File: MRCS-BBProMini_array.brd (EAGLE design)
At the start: 107.5 x 110 mm, 30 parts

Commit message: fixed silkscreen
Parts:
- ARDUINO1X11, ARDUINO1X12, ARDUINO1X13: value (none) -> ARDUINO_PRO_MINI_DAVEK
- BBLEOX11, BBLEOX12, BBLEOX13: value (none) -> Footprint
- C1X11, C1X12, C1X13: device SPCoast:e5-10.5 -> SPCoast:E5-10.5
- C2X11, C2X12, C2X13: value (none) -> 1.0uF
- C3X11, C3X12, C3X13: value (none) -> 10uF
- J1X11, J1X12, J1X13: value (none) -> 2.1mm
- VR5.0X11, VR5.0X12, VR5.0X13: value (none) -> 5v
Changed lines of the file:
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@@
 <layer number="23" name="tOrigins" color="15" fill="1" visible="yes" active="yes"/>
 <layer number="24" name="bOrigins" color="15" fill="1" visible="no" active="yes"/>
-<layer number="25" name="tNames" color="7" fill="1" visible="no" active="yes"/>
+<layer number="25" name="tNames" color="7" fill="1" visible="yes" active="yes"/>
 <layer number="26" name="bNames" color="7" fill="1" visible="no" active="yes"/>
-<layer number="27" name="tValues" color="7" fill="1" visible="no" active="yes"/>
+<layer number="27" name="tValues" color="7" fill="1" visible="yes" active="yes"/>
 <layer number="28" name="bValues" color="7" fill="1" visible="no" active="yes"/>
 <layer number="29" name="tStop" color="7" fill="3" visible="no" active="yes"/>
@@
 <layer number="46" name="Milling" color="3" fill="1" visible="yes" active="yes"/>
 <layer number="47" name="Measures" color="7" fill="1" visible="yes" active="yes"/>
-<layer number="48" name="Document" color="7" fill="1" visible="no" active="yes"/>
+<layer number="48" name="Document" color="7" fill="1" visible="yes" active="yes"/>
 <layer number="49" name="Reference" color="7" fill="1" visible="yes" active="yes"/>
 <layer number="50" name="dxf" color="7" fill="1" visible="no" active="no"/>
@@
 <layer number="102" name="Changes" color="13" fill="1" visible="yes" active="yes"/>
 <layer number="103" name="tMap" color="29" fill="4" visible="no" active="yes"/>
-<layer number="104" name="Name" color="16" fill="1" visible="no" active="yes"/>
+<layer number="104" name="Name" color="16" fill="1" visible="yes" active="yes"/>
 <layer number="105" name="tPlate" color="7" fill="1" visible="no" active="yes"/>
 <layer number="106" name="bPlate" color="7" fill="1" visible="no" active="yes"/>
@@
 <layer number="123" name="tTestmark" color="7" fill="1" visible="no" active="yes"/>
 <layer number="124" name="bTestmark" color="7" fill="1" visible="no" active="yes"/>
-<layer number="125" name="_tNames" color="14" fill="1" visible="yes" active="yes"/>
+<layer number="125" name="_tNames" color="14" fill="1" visible="no" active="yes"/>
 <layer number="126" name="_bNames" color="7" fill="1" visible="no" active="yes"/>
 <layer number="127" name="_tValues" color="7" fill="1" visible="no" active="no"/>
@@
 </autorouter>
 <elements>
-<element name="ARDUINO1X11" library="SPCoast" package="ARDUINO_PRO_MINI_DAVEK" value="" x="39.37" y="26.67" rot="R270"/>
-<element name="BBLEOX11" library="SPCoast" package="ARDUINO-BBLEO" value="" x="0" y="0"/>
-<element name="C1X11" library="SPCoast" package="e5-10.5" value="" x="15.875" y="18.415" rot="R90"/>
-<element name="C2X11" library="SPCoast" package="C050-024X044" value="" x="3.175" y="27.305" rot="R90"/>
-<element name="C3X11" library="SPCoast" package="C050-024X044" value="" x="3.175" y="19.685" rot="R270"/>
-<element name="J1X11" library="SPCoast" package="DCJ0202" value="" x="8.89" y="9.525" rot="R270"/>
+<element name="ARDUINO1X11" library="SPCoast" package="ARDUINO_PRO_MINI_DAVEK" value="ARDUINO_PRO_MINI_DAVEK" x="39.37" y="26.67" rot="R270"/>
+<element name="BBLEOX11" library="SPCoast" package="ARDUINO-BBLEO" value="Footprint" x="0" y="0"/>
+<element name="C1X11" library="SPCoast" package="E5-10.5" value="" x="15.875" y="18.415" rot="R90"/>
+<element name="C2X11" library="SPCoast" package="C050-024X044" value="1.0uF" x="3.175" y="27.305" rot="R90"/>
+<element name="C3X11" library="SPCoast" package="C050-024X044" value="10uF" x="3.175" y="19.685" rot="R270"/>
+<element name="J1X11" library="SPCoast" package="DCJ0202" value="2.1mm" x="8.89" y="9.525" rot="R270"/>
 <element name="JP1X11" library="SPCoast" package="SJ_2S-NO" value="" x="60.96" y="4.445" rot="R90"/>
 <element name="LABEL1X11" library="SPCoast" package="PWR_LABEL" value="" x="20.32" y="6.985" rot="R90"/>
 <element name="OSHW1X11" library="SPCoast" package="OSHW-LOGO-M" value="" x="34.29" y="11.43"/>
-<element name="VR5.0X11" library="SPCoast" package="TO-220-RA-SINK" value="" x="6.35" y="23.495" rot="R270"/>
-<element name="ARDUINO1X12" library="SPCoast" package="ARDUINO_PRO_MINI_DAVEK" value="" x="39.37" y="59.944" rot="R270"/>
-<element name="BBLEOX12" library="SPCoast" package="ARDUINO-BBLEO" value="" x="0" y="33.274"/>
-<element name="C1X12" library="SPCoast" package="e5-10.5" value="" x="15.875" y="51.689" rot="R90"/>
-<element name="C2X12" library="SPCoast" package="C050-024X044" value="" x="3.175" y="60.579" rot="R90"/>
-<element name="C3X12" library="SPCoast" package="C050-024X044" value="" x="3.175" y="52.959" rot="R270"/>
-<element name="J1X12" library="SPCoast" package="DCJ0202" value="" x="8.89" y="42.799" rot="R270"/>
+<element name="VR5.0X11" library="SPCoast" package="TO-220-RA-SINK" value="5v" x="6.35" y="23.495" rot="R270"/>
+<element name="ARDUINO1X12" library="SPCoast" package="ARDUINO_PRO_MINI_DAVEK" value="ARDUINO_PRO_MINI_DAVEK" x="39.37" y="59.944" rot="R270"/>
+<element name="BBLEOX12" library="SPCoast" package="ARDUINO-BBLEO" value="Footprint" x="0" y="33.274"/>
+<element name="C1X12" library="SPCoast" package="E5-10.5" value="" x="15.875" y="51.689" rot="R90"/>
+<element name="C2X12" library="SPCoast" package="C050-024X044" value="1.0uF" x="3.175" y="60.579" rot="R90"/>
+<element name="C3X12" library="SPCoast" package="C050-024X044" value="10uF" x="3.175" y="52.959" rot="R270"/>
+<element name="J1X12" library="SPCoast" package="DCJ0202" value="2.1mm" x="8.89" y="42.799" rot="R270"/>
 <element name="JP1X12" library="SPCoast" package="SJ_2S-NO" value="" x="60.96" y="37.719" rot="R90"/>
 <element name="LABEL1X12" library="SPCoast" package="PWR_LABEL" value="" x="20.32" y="40.259" rot="R90"/>
 <element name="OSHW1X12" library="SPCoast" package="OSHW-LOGO-M" value="" x="34.29" y="44.704"/>
-<element name="VR5.0X12" library="SPCoast" package="TO-220-RA-SINK" value="" x="6.35" y="56.769" rot="R270"/>
-<element name="ARDUINO1X13" library="SPCoast" package="ARDUINO_PRO_MINI_DAVEK" value="" x="39.37" y="93.218" rot="R270"/>
-<element name="BBLEOX13" library="SPCoast" package="ARDUINO-BBLEO" value="" x="0" y="66.548"/>
-<element name="C1X13" library="SPCoast" package="e5-10.5" value="" x="15.875" y="84.963" rot="R90"/>
-<element name="C2X13" library="SPCoast" package="C050-024X044" value="" x="3.175" y="93.853" rot="R90"/>
-<element name="C3X13" library="SPCoast" package="C050-024X044" value="" x="3.175" y="86.233" rot="R270"/>
-<element name="J1X13" library="SPCoast" package="DCJ0202" value="" x="8.89" y="76.073" rot="R270"/>
+<element name="VR5.0X12" library="SPCoast" package="TO-220-RA-SINK" value="5v" x="6.35" y="56.769" rot="R270"/>
+<element name="ARDUINO1X13" library="SPCoast" package="ARDUINO_PRO_MINI_DAVEK" value="ARDUINO_PRO_MINI_DAVEK" x="39.37" y="93.218" rot="R270"/>
+<element name="BBLEOX13" library="SPCoast" package="ARDUINO-BBLEO" value="Footprint" x="0" y="66.548"/>
+<element name="C1X13" library="SPCoast" package="E5-10.5" value="" x="15.875" y="84.963" rot="R90"/>
+<element name="C2X13" library="SPCoast" package="C050-024X044" value="1.0uF" x="3.175" y="93.853" rot="R90"/>
+<element name="C3X13" library="SPCoast" package="C050-024X044" value="10uF" x="3.175" y="86.233" rot="R270"/>
+<element name="J1X13" library="SPCoast" package="DCJ0202" value="2.1mm" x="8.89" y="76.073" rot="R270"/>
 <element name="JP1X13" library="SPCoast" package="SJ_2S-NO" value="" x="60.96" y="70.993" rot="R90"/>
 <element name="LABEL1X13" library="SPCoast" package="PWR_LABEL" value="" x="20.32" y="73.533" rot="R90"/>
 <element name="OSHW1X13" library="SPCoast" package="OSHW-LOGO-M" value="" x="34.29" y="77.978"/>
-<element name="VR5.0X13" library="SPCoast" package="TO-220-RA-SINK" value="" x="6.35" y="90.043" rot="R270"/>
+<element name="VR5.0X13" library="SPCoast" package="TO-220-RA-SINK" value="5v" x="6.35" y="90.043" rot="R270"/>
 </elements>
 <signals>

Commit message: fixed silkscreen
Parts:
- C1X11, C1X12, C1X13: value (none) -> 150uF
- JP1X11, JP1X12, JP1X13: value (none) -> OFF
- LABEL1X11, LABEL1X12, LABEL1X13: value (none) -> 7-12vDC
- OSHW1X11, OSHW1X12, OSHW1X13: value (none) -> OSHW
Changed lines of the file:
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@@
 <element name="ARDUINO1X11" library="SPCoast" package="ARDUINO_PRO_MINI_DAVEK" value="ARDUINO_PRO_MINI_DAVEK" x="39.37" y="26.67" rot="R270"/>
 <element name="BBLEOX11" library="SPCoast" package="ARDUINO-BBLEO" value="Footprint" x="0" y="0"/>
-<element name="C1X11" library="SPCoast" package="E5-10.5" value="" x="15.875" y="18.415" rot="R90"/>
+<element name="C1X11" library="SPCoast" package="E5-10.5" value="150uF" x="15.875" y="18.415" rot="R90"/>
 <element name="C2X11" library="SPCoast" package="C050-024X044" value="1.0uF" x="3.175" y="27.305" rot="R90"/>
 <element name="C3X11" library="SPCoast" package="C050-024X044" value="10uF" x="3.175" y="19.685" rot="R270"/>
 <element name="J1X11" library="SPCoast" package="DCJ0202" value="2.1mm" x="8.89" y="9.525" rot="R270"/>
-<element name="JP1X11" library="SPCoast" package="SJ_2S-NO" value="" x="60.96" y="4.445" rot="R90"/>
-<element name="LABEL1X11" library="SPCoast" package="PWR_LABEL" value="" x="20.32" y="6.985" rot="R90"/>
-<element name="OSHW1X11" library="SPCoast" package="OSHW-LOGO-M" value="" x="34.29" y="11.43"/>
+<element name="JP1X11" library="SPCoast" package="SJ_2S-NO" value="OFF" x="60.96" y="4.445" rot="R90"/>
+<element name="LABEL1X11" library="SPCoast" package="PWR_LABEL" value="7-12vDC" x="20.32" y="6.985" rot="R90"/>
+<element name="OSHW1X11" library="SPCoast" package="OSHW-LOGO-M" value="OSHW" x="34.29" y="11.43"/>
 <element name="VR5.0X11" library="SPCoast" package="TO-220-RA-SINK" value="5v" x="6.35" y="23.495" rot="R270"/>
 <element name="ARDUINO1X12" library="SPCoast" package="ARDUINO_PRO_MINI_DAVEK" value="ARDUINO_PRO_MINI_DAVEK" x="39.37" y="59.944" rot="R270"/>
 <element name="BBLEOX12" library="SPCoast" package="ARDUINO-BBLEO" value="Footprint" x="0" y="33.274"/>
-<element name="C1X12" library="SPCoast" package="E5-10.5" value="" x="15.875" y="51.689" rot="R90"/>
+<element name="C1X12" library="SPCoast" package="E5-10.5" value="150uF" x="15.875" y="51.689" rot="R90"/>
 <element name="C2X12" library="SPCoast" package="C050-024X044" value="1.0uF" x="3.175" y="60.579" rot="R90"/>
 <element name="C3X12" library="SPCoast" package="C050-024X044" value="10uF" x="3.175" y="52.959" rot="R270"/>
 <element name="J1X12" library="SPCoast" package="DCJ0202" value="2.1mm" x="8.89" y="42.799" rot="R270"/>
-<element name="JP1X12" library="SPCoast" package="SJ_2S-NO" value="" x="60.96" y="37.719" rot="R90"/>
-<element name="LABEL1X12" library="SPCoast" package="PWR_LABEL" value="" x="20.32" y="40.259" rot="R90"/>
-<element name="OSHW1X12" library="SPCoast" package="OSHW-LOGO-M" value="" x="34.29" y="44.704"/>
+<element name="JP1X12" library="SPCoast" package="SJ_2S-NO" value="OFF" x="60.96" y="37.719" rot="R90"/>
+<element name="LABEL1X12" library="SPCoast" package="PWR_LABEL" value="7-12vDC" x="20.32" y="40.259" rot="R90"/>
+<element name="OSHW1X12" library="SPCoast" package="OSHW-LOGO-M" value="OSHW" x="34.29" y="44.704"/>
 <element name="VR5.0X12" library="SPCoast" package="TO-220-RA-SINK" value="5v" x="6.35" y="56.769" rot="R270"/>
 <element name="ARDUINO1X13" library="SPCoast" package="ARDUINO_PRO_MINI_DAVEK" value="ARDUINO_PRO_MINI_DAVEK" x="39.37" y="93.218" rot="R270"/>
 <element name="BBLEOX13" library="SPCoast" package="ARDUINO-BBLEO" value="Footprint" x="0" y="66.548"/>
-<element name="C1X13" library="SPCoast" package="E5-10.5" value="" x="15.875" y="84.963" rot="R90"/>
+<element name="C1X13" library="SPCoast" package="E5-10.5" value="150uF" x="15.875" y="84.963" rot="R90"/>
 <element name="C2X13" library="SPCoast" package="C050-024X044" value="1.0uF" x="3.175" y="93.853" rot="R90"/>
 <element name="C3X13" library="SPCoast" package="C050-024X044" value="10uF" x="3.175" y="86.233" rot="R270"/>
 <element name="J1X13" library="SPCoast" package="DCJ0202" value="2.1mm" x="8.89" y="76.073" rot="R270"/>
-<element name="JP1X13" library="SPCoast" package="SJ_2S-NO" value="" x="60.96" y="70.993" rot="R90"/>
-<element name="LABEL1X13" library="SPCoast" package="PWR_LABEL" value="" x="20.32" y="73.533" rot="R90"/>
-<element name="OSHW1X13" library="SPCoast" package="OSHW-LOGO-M" value="" x="34.29" y="77.978"/>
+<element name="JP1X13" library="SPCoast" package="SJ_2S-NO" value="OFF" x="60.96" y="70.993" rot="R90"/>
+<element name="LABEL1X13" library="SPCoast" package="PWR_LABEL" value="7-12vDC" x="20.32" y="73.533" rot="R90"/>
+<element name="OSHW1X13" library="SPCoast" package="OSHW-LOGO-M" value="OSHW" x="34.29" y="77.978"/>
 <element name="VR5.0X13" library="SPCoast" package="TO-220-RA-SINK" value="5v" x="6.35" y="90.043" rot="R270"/>
 </elements>

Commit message: normalized values
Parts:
- ARDUINO1X11, ARDUINO1X12, ARDUINO1X13: value ARDUINO_PRO_MINI_DAVEK -> DAVEK
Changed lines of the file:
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@@
 </autorouter>
 <elements>
-<element name="ARDUINO1X11" library="SPCoast" package="ARDUINO_PRO_MINI_DAVEK" value="ARDUINO_PRO_MINI_DAVEK" x="39.37" y="26.67" rot="R270"/>
+<element name="ARDUINO1X11" library="SPCoast" package="ARDUINO_PRO_MINI_DAVEK" value="DAVEK" x="39.37" y="26.67" rot="R270"/>
 <element name="BBLEOX11" library="SPCoast" package="ARDUINO-BBLEO" value="Footprint" x="0" y="0"/>
 <element name="C1X11" library="SPCoast" package="E5-10.5" value="150uF" x="15.875" y="18.415" rot="R90"/>
@@
 <element name="OSHW1X11" library="SPCoast" package="OSHW-LOGO-M" value="OSHW" x="34.29" y="11.43"/>
 <element name="VR5.0X11" library="SPCoast" package="TO-220-RA-SINK" value="5v" x="6.35" y="23.495" rot="R270"/>
-<element name="ARDUINO1X12" library="SPCoast" package="ARDUINO_PRO_MINI_DAVEK" value="ARDUINO_PRO_MINI_DAVEK" x="39.37" y="59.944" rot="R270"/>
+<element name="ARDUINO1X12" library="SPCoast" package="ARDUINO_PRO_MINI_DAVEK" value="DAVEK" x="39.37" y="59.944" rot="R270"/>
 <element name="BBLEOX12" library="SPCoast" package="ARDUINO-BBLEO" value="Footprint" x="0" y="33.274"/>
 <element name="C1X12" library="SPCoast" package="E5-10.5" value="150uF" x="15.875" y="51.689" rot="R90"/>
@@
 <element name="OSHW1X12" library="SPCoast" package="OSHW-LOGO-M" value="OSHW" x="34.29" y="44.704"/>
 <element name="VR5.0X12" library="SPCoast" package="TO-220-RA-SINK" value="5v" x="6.35" y="56.769" rot="R270"/>
-<element name="ARDUINO1X13" library="SPCoast" package="ARDUINO_PRO_MINI_DAVEK" value="ARDUINO_PRO_MINI_DAVEK" x="39.37" y="93.218" rot="R270"/>
+<element name="ARDUINO1X13" library="SPCoast" package="ARDUINO_PRO_MINI_DAVEK" value="DAVEK" x="39.37" y="93.218" rot="R270"/>
 <element name="BBLEOX13" library="SPCoast" package="ARDUINO-BBLEO" value="Footprint" x="0" y="66.548"/>
 <element name="C1X13" library="SPCoast" package="E5-10.5" value="150uF" x="15.875" y="84.963" rot="R90"/>

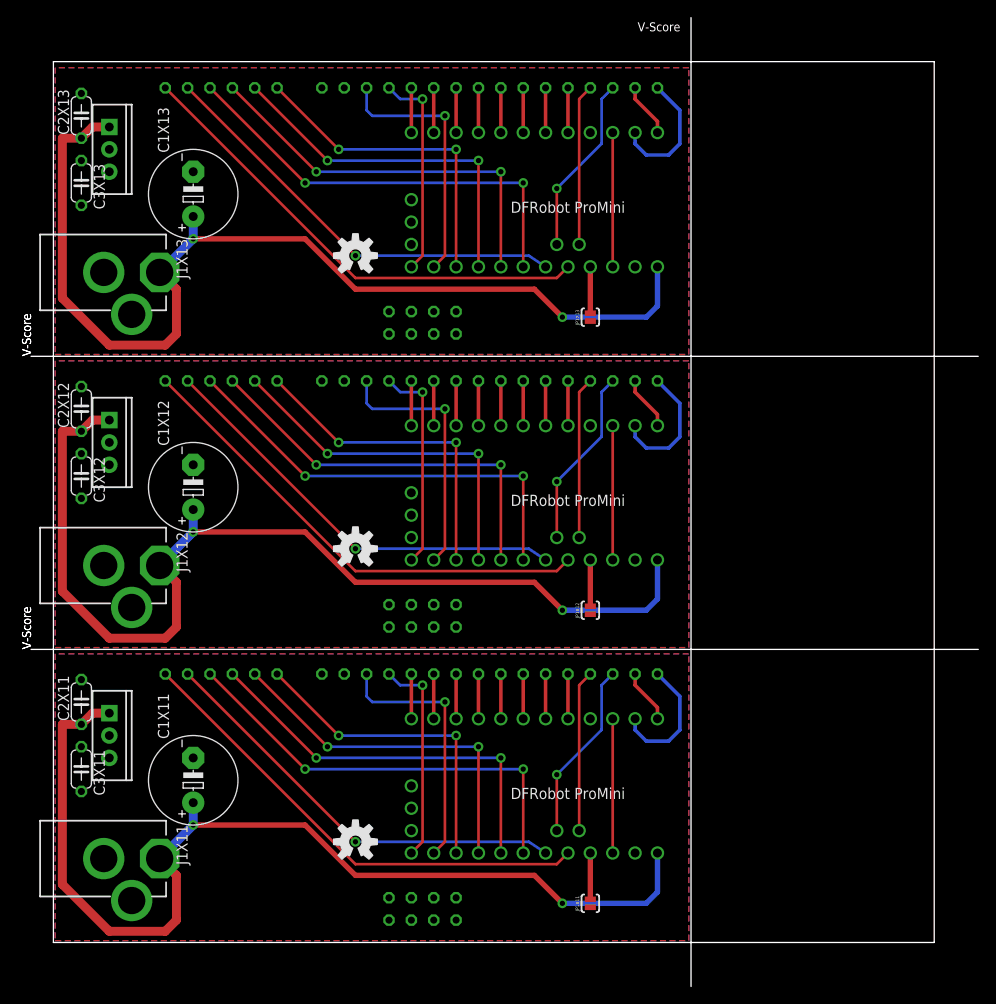
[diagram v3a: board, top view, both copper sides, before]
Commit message: Add 2k2 pullup to pin13
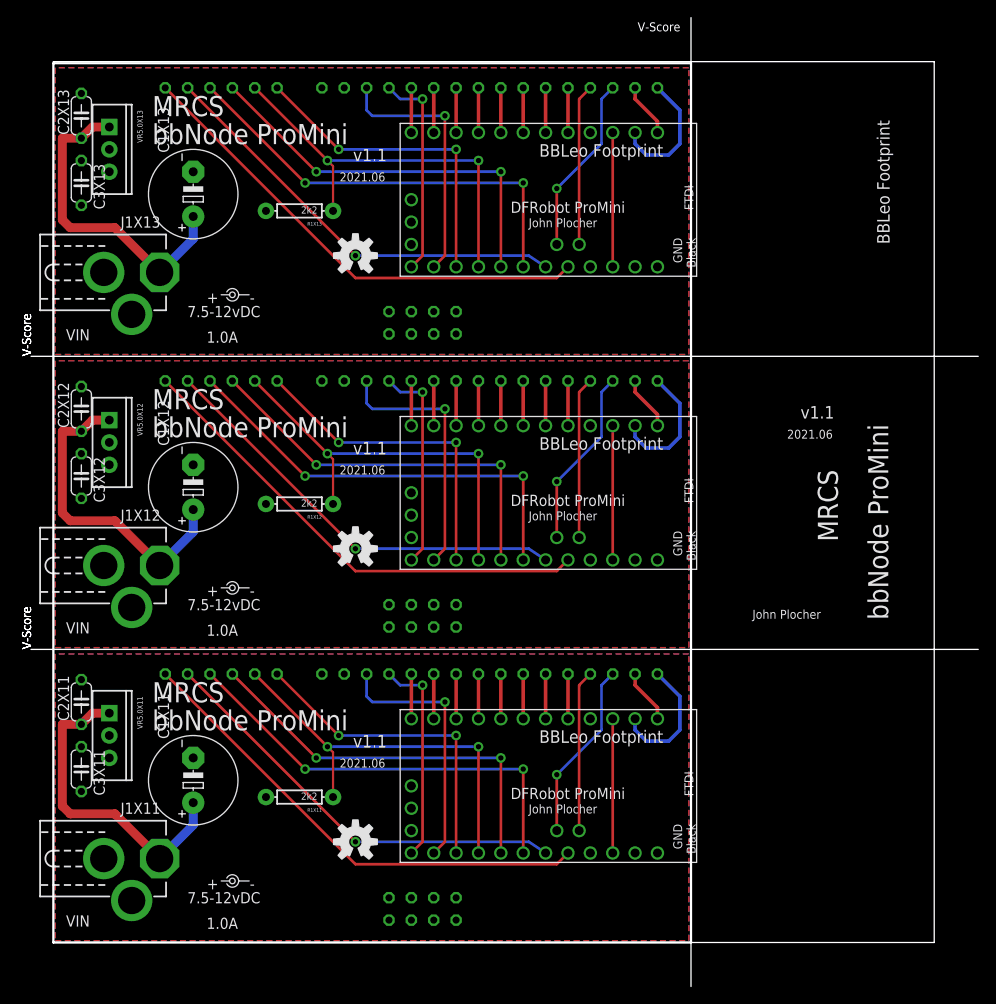
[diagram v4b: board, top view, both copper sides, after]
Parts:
- removed JP1X11, JP1X12, JP1X13: OFF, SPCoast:SJ_2S-NO
- added R1X11, R1X12, R1X13: 2k2, SPCoast:AXIAL-0.3-RES
- LABEL1X11, LABEL1X12, LABEL1X13: value 7-12vDC -> 7.5-12vDC
- VR5.0X11, VR5.0X12, VR5.0X13: device SPCoast:TO-220-RA-SINK -> SPCoast:TO-220-RA
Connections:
- removed net N$1X11: ARDUINO1X11.5V, JP1X11.2
- removed net N$1X12: ARDUINO1X12.5V, JP1X12.2
- removed net N$1X13: ARDUINO1X13.5V, JP1X13.2
- net +9VX11: no longer ARDUINO1X11.VIN
- net +9VX12: no longer ARDUINO1X12.VIN
- net +9VX13: no longer ARDUINO1X13.VIN
- net GPB3X11: now also R1X11.P$1
- net GPB3X12: now also R1X12.P$1
- net GPB3X13: now also R1X13.P$1
- net VCCIOX11: now also ARDUINO1X11.5V, R1X11.P$2; no longer JP1X11.1
- net VCCIOX12: now also ARDUINO1X12.5V, R1X12.P$2; no longer JP1X12.1
- net VCCIOX13: now also ARDUINO1X13.5V, R1X13.P$2; no longer JP1X13.1
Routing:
- net +9VX13: track 116.8 -> 36.6 mm, vias 2 -> 0
- net +9VX12: track 116.8 -> 36.6 mm, vias 2 -> 0
- net +9VX11: track 116.8 -> 36.6 mm, vias 2 -> 0
- net GPB3X12: track 40.9 -> 46.9 mm
- net GPB3X11: track 40.9 -> 46.9 mm
- net GPB3X13: track 40.9 -> 46.9 mm
- net N$1X13: track 5.27 -> 0.00 mm
- net N$1X12: track 5.27 -> 0.00 mm
- net N$1X11: track 5.27 -> 0.00 mm
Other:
- outline, holes or cut-outs redrawn
- board text added: "1.0A"
- board text added: "2021.06"
- board text added: "Made in the PCR, Coast Division, NMRA"
- board text added: "R1"
- board text added: "bbNode Pro Mini"
- board text added: "v1.1"
- board text removed: "2019.08"
- board text removed: "7-12vDC 1.0A"
- board text removed: "Coast Division, NMRA'"
- board text removed: "JP1"
- board text removed: "Pro Mini'"
- board text removed: "v1.0"
